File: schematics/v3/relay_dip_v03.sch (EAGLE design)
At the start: 51 parts, among them IC1 74HCT04D, P1 696-SML-0805ICTR, P2 696-SML-0805ICTR, P3 696-SML-0805ICTR, P4 696-SML-0805ICTR, U1 DS2431P+T&R

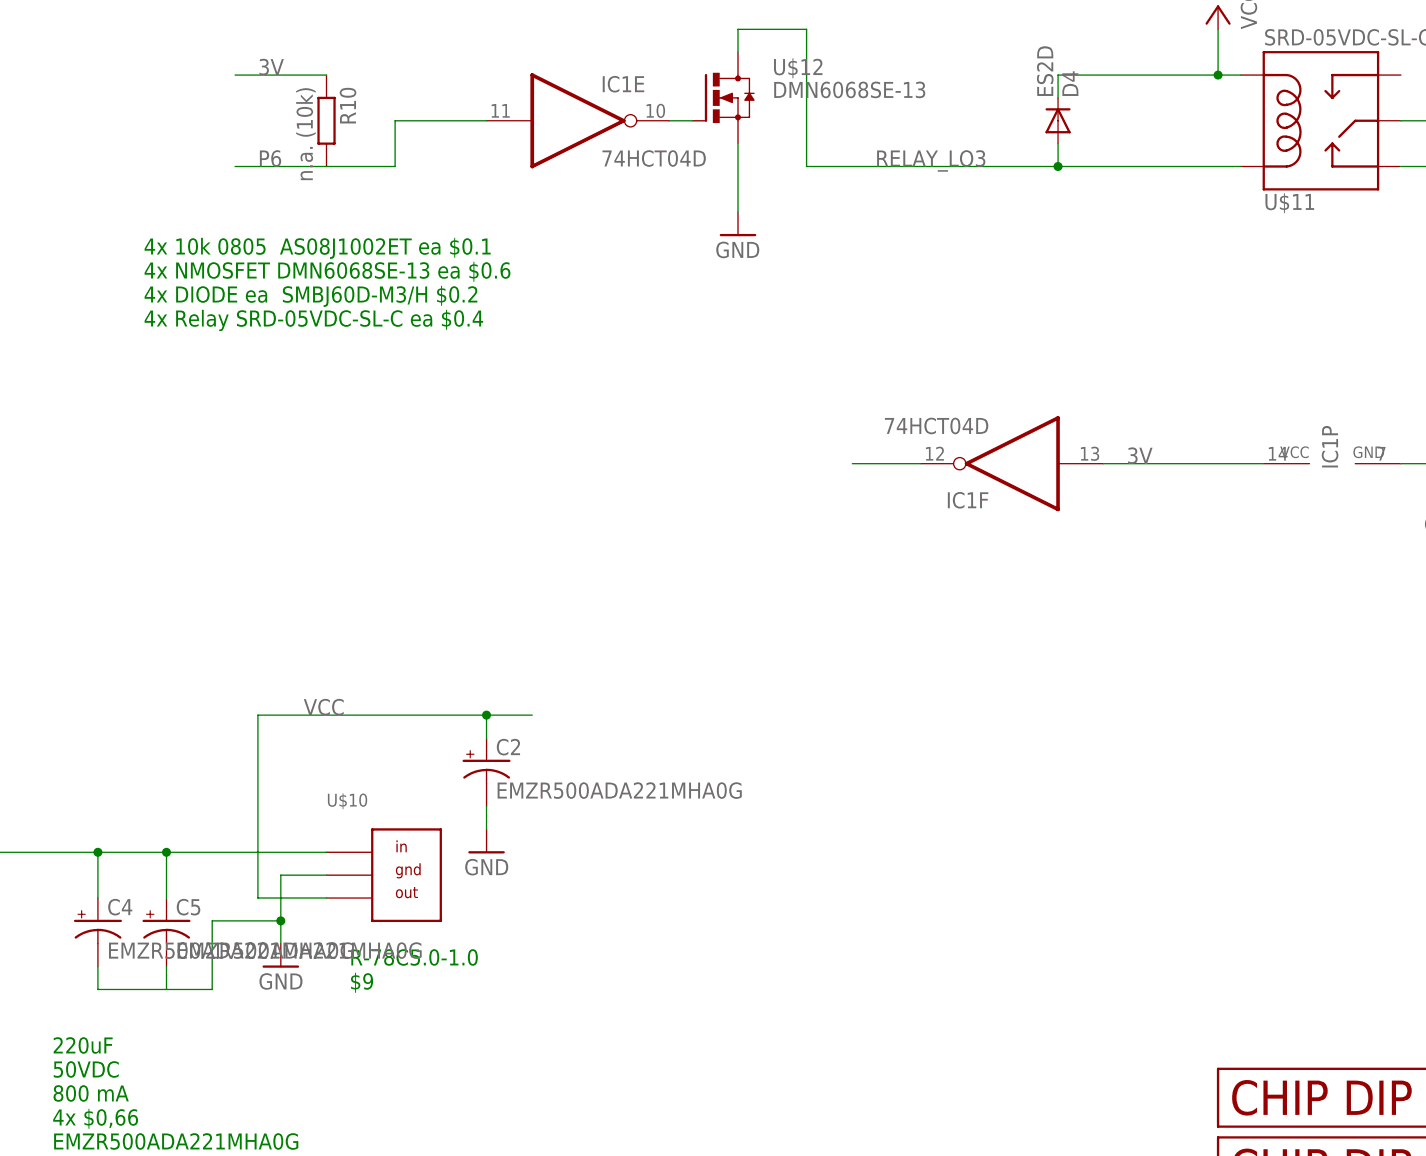
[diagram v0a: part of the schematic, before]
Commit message: added v3, fixed ds2431 footprint, added quotation
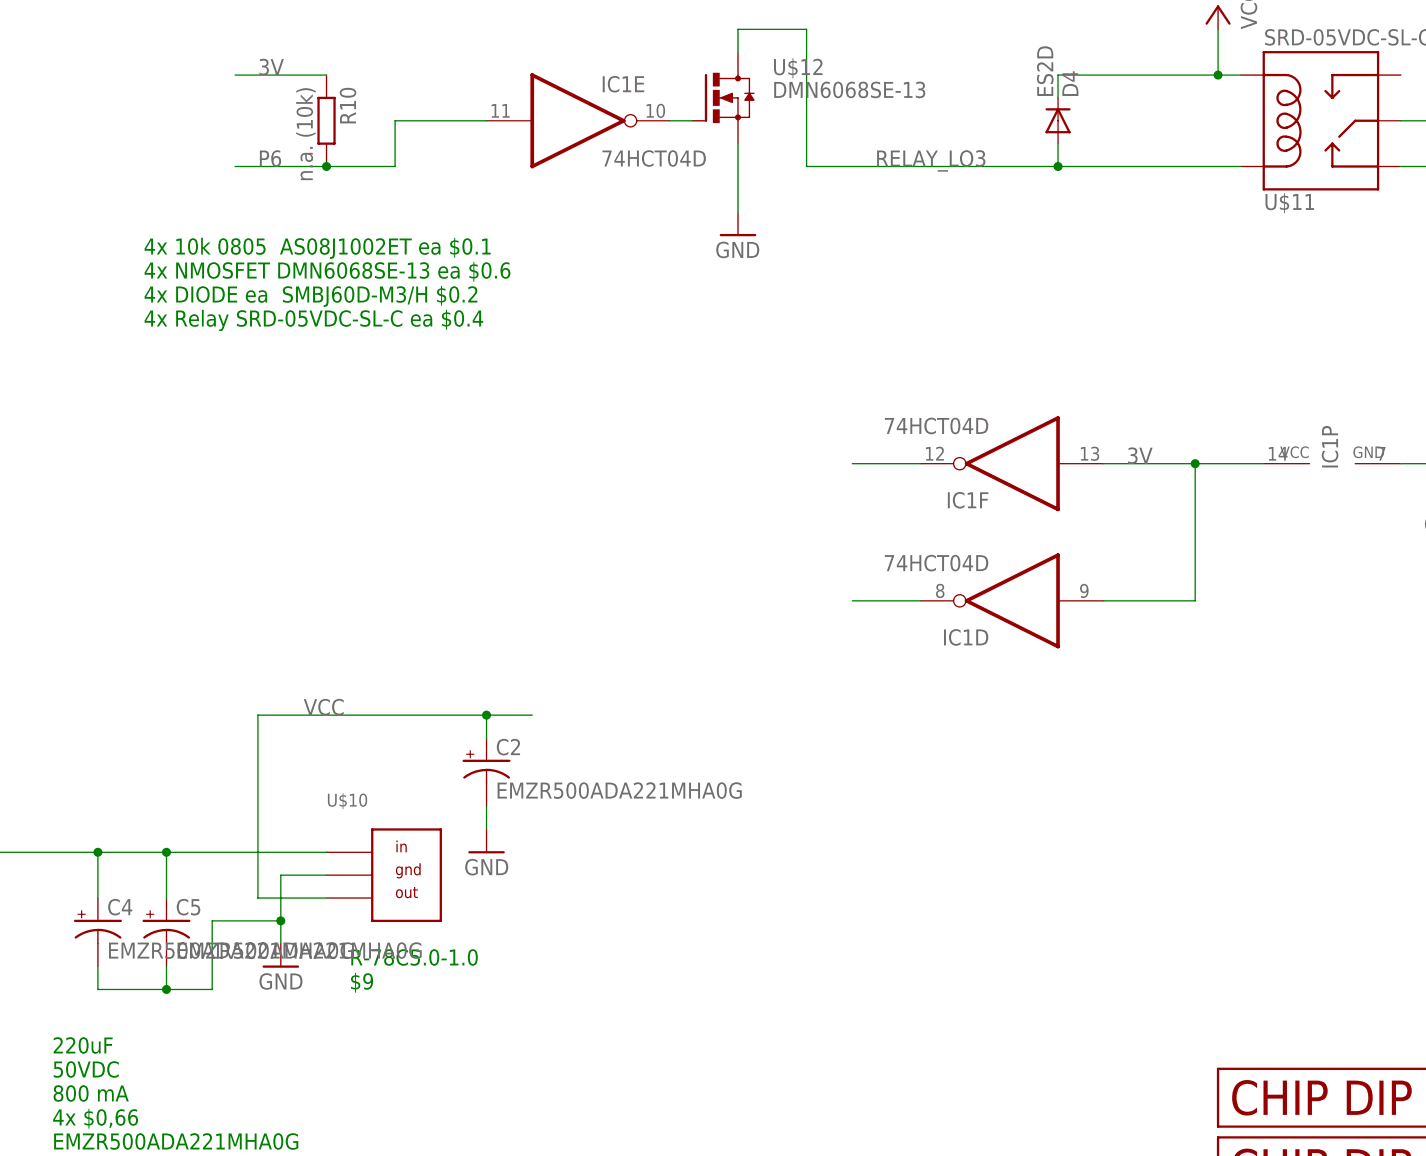
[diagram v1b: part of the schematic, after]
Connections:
- new net N$12: IC1D.O
- net 3V: now also IC1D.I
- net LD2: now also U1.IO
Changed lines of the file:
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@@
 <instance part="GND8" gate="1" x="195.58" y="414.02"/>
 <instance part="U1" gate="G$1" x="20.32" y="457.2" rot="MR0"/>
+<instance part="IC1" gate="D" x="147.32" y="403.86" rot="R180"/>
 </instances>
 <busses>
@@
 <wire x1="58.42" y1="368.3" x2="66.04" y2="368.3" width="0.1524" layer="91"/>
 <junction x="66.04" y="368.3"/>
+<junction x="53.34" y="360.68"/>
 </segment>
 <segment>
@@
 <junction x="2.54" y="459.74"/>
 <pinref part="JP1" gate="G$1" pin="2"/>
+<pinref part="U1" gate="G$1" pin="IO"/>
 </segment>
 </net>
@@
 <wire x1="71.12" y1="452.12" x2="60.96" y2="452.12" width="0.1524" layer="91"/>
 <label x="63.5" y="452.12" size="1.778" layer="95"/>
+<junction x="71.12" y="452.12"/>
 </segment>
 </net>
@@
 <segment>
 <pinref part="IC1" gate="P" pin="VCC"/>
-<wire x1="175.26" y1="419.1" x2="157.48" y2="419.1" width="0.1524" layer="91"/>
+<wire x1="175.26" y1="419.1" x2="167.64" y2="419.1" width="0.1524" layer="91"/>
 <label x="160.02" y="419.1" size="1.778" layer="95"/>
 <pinref part="IC1" gate="F" pin="I"/>
+<pinref part="IC1" gate="D" pin="I"/>
+<wire x1="167.64" y1="419.1" x2="157.48" y2="419.1" width="0.1524" layer="91"/>
+<wire x1="157.48" y1="403.86" x2="167.64" y2="403.86" width="0.1524" layer="91"/>
+<wire x1="167.64" y1="403.86" x2="167.64" y2="419.1" width="0.1524" layer="91"/>
+<junction x="167.64" y="419.1"/>
 </segment>
 </net>
@@
 </segment>
 </net>
+<net name="N$12" class="0">
+<segment>
+<pinref part="IC1" gate="D" pin="O"/>
+<wire x1="137.16" y1="403.86" x2="129.54" y2="403.86" width="0.1524" layer="91"/>
+</segment>
+</net>

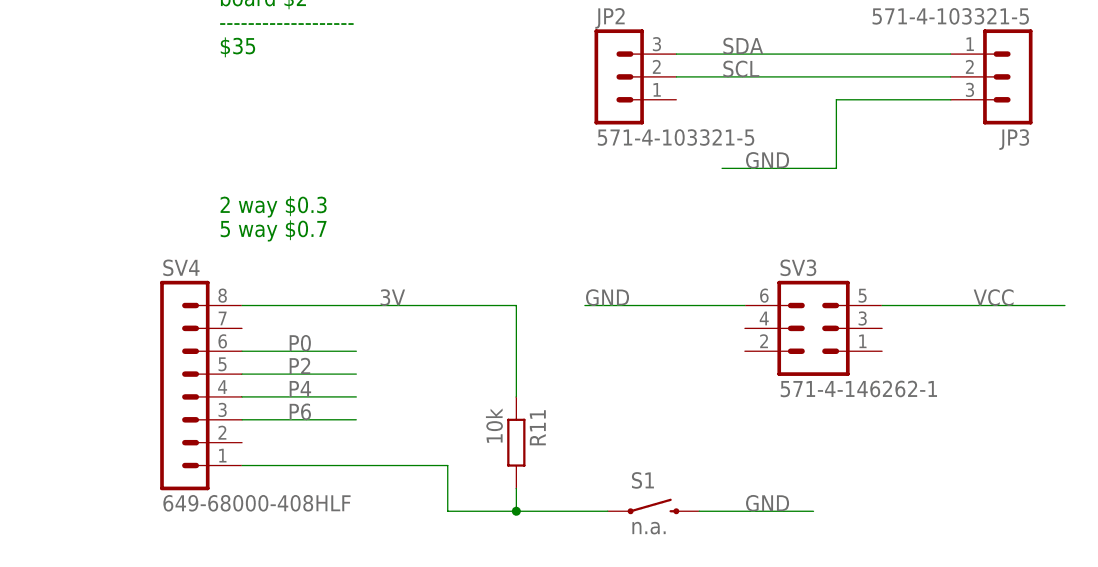
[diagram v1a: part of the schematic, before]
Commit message: flipped pin header to lower layer
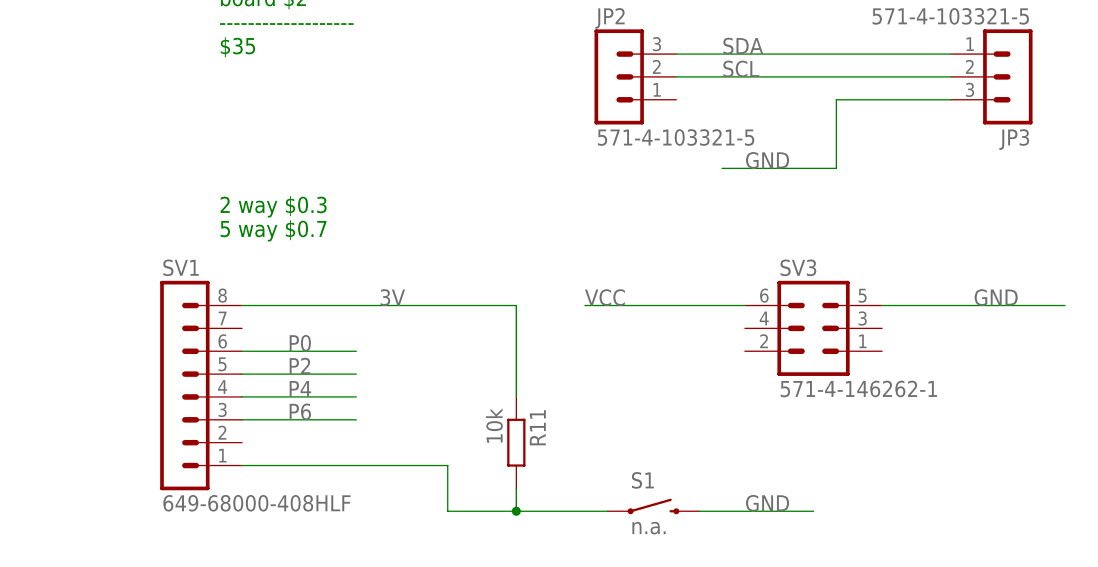
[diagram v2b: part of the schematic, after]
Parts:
- renumbered SV4 to SV1
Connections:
- net GND: now also SV3.5; no longer SV3.6
- net VCC: now also SV3.6; no longer SV3.5
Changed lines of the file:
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@@
 <part name="S1" library="SparkFun-Electromechanical" deviceset="SWITCH-MOMENTARY-2" device="SMD" value="n.a."/>
 <part name="R11" library="rcl" deviceset="R-EU_" device="R0805" value="10k"/>
-<part name="SV4" library="con-lstb" deviceset="MA08-1" device="" value="649-68000-408HLF"/>
 <part name="JP2" library="con-lstb" deviceset="MA03-1" device="" value="571-4-103321-5"/>
 <part name="JP3" library="con-lstb" deviceset="MA03-1" device="" value="571-4-103321-5"/>
@@
 <part name="GND8" library="supply1" deviceset="GND" device=""/>
 <part name="U1" library="JKW_CHIP" deviceset="DS2431" device="P" value="DS2431P+T&amp;R"/>
+<part name="SV1" library="con-lstb" deviceset="MA08-1" device="" value="649-68000-408HLF"/>
 </parts>
 <sheets>
@@
 <instance part="S1" gate="G$1" x="299.72" y="500.38"/>
 <instance part="R11" gate="G$1" x="284.48" y="508" rot="R270"/>
-<instance part="SV4" gate="1" x="246.38" y="513.08"/>
 <instance part="JP2" gate="G$1" x="294.64" y="548.64"/>
 <instance part="JP3" gate="G$1" x="340.36" y="548.64" rot="R180"/>
@@
 <instance part="U1" gate="G$1" x="20.32" y="457.2" rot="MR0"/>
 <instance part="IC1" gate="D" x="147.32" y="403.86" rot="R180"/>
+<instance part="SV1" gate="1" x="246.38" y="513.08"/>
 </instances>
 <busses>
@@
 </segment>
 <segment>
-<pinref part="SV3" gate="1" pin="6"/>
-<wire x1="309.88" y1="523.24" x2="292.1" y2="523.24" width="0.1524" layer="91"/>
-<label x="292.1" y="523.24" size="1.778" layer="95"/>
-</segment>
-<segment>
 <pinref part="GND7" gate="1" pin="GND"/>
 <pinref part="C2" gate="G$1" pin="-"/>
@@
 <wire x1="195.58" y1="419.1" x2="190.5" y2="419.1" width="0.1524" layer="91"/>
 </segment>
+<segment>
+<pinref part="SV3" gate="1" pin="5"/>
+<wire x1="325.12" y1="523.24" x2="345.44" y2="523.24" width="0.1524" layer="91"/>
+<label x="335.28" y="523.24" size="1.778" layer="95"/>
+</segment>
 </net>
 <net name="P0" class="0">
@@
 <wire x1="254" y1="518.16" x2="266.7" y2="518.16" width="0.1524" layer="91"/>
 <label x="259.08" y="518.16" size="1.778" layer="95"/>
-<pinref part="SV4" gate="1" pin="6"/>
+<pinref part="SV1" gate="1" pin="6"/>
 </segment>
 <segment>
@@
 </segment>
 <segment>
-<pinref part="SV3" gate="1" pin="5"/>
-<wire x1="325.12" y1="523.24" x2="345.44" y2="523.24" width="0.1524" layer="91"/>
-<label x="335.28" y="523.24" size="1.778" layer="95"/>
-</segment>
-<segment>
 <pinref part="U$10" gate="G$1" pin="OUT"/>
 <wire x1="71.12" y1="370.84" x2="63.5" y2="370.84" width="0.1524" layer="91"/>
@@
 <wire x1="88.9" y1="388.62" x2="88.9" y2="391.16" width="0.1524" layer="91"/>
 <junction x="88.9" y="391.16"/>
+</segment>
+<segment>
+<pinref part="SV3" gate="1" pin="6"/>
+<wire x1="309.88" y1="523.24" x2="292.1" y2="523.24" width="0.1524" layer="91"/>
+<label x="292.1" y="523.24" size="1.778" layer="95"/>
 </segment>
 </net>
@@
 <wire x1="254" y1="515.62" x2="266.7" y2="515.62" width="0.1524" layer="91"/>
 <label x="259.08" y="515.62" size="1.778" layer="95"/>
-<pinref part="SV4" gate="1" pin="5"/>
+<pinref part="SV1" gate="1" pin="5"/>
 </segment>
 <segment>
@@
 <wire x1="254" y1="513.08" x2="266.7" y2="513.08" width="0.1524" layer="91"/>
 <label x="259.08" y="513.08" size="1.778" layer="95"/>
-<pinref part="SV4" gate="1" pin="4"/>
+<pinref part="SV1" gate="1" pin="4"/>
 </segment>
 <segment>
@@
 <wire x1="254" y1="510.54" x2="266.7" y2="510.54" width="0.1524" layer="91"/>
 <label x="259.08" y="510.54" size="1.778" layer="95"/>
-<pinref part="SV4" gate="1" pin="3"/>
+<pinref part="SV1" gate="1" pin="3"/>
 </segment>
 <segment>
@@
 <wire x1="284.48" y1="502.92" x2="284.48" y2="500.38" width="0.1524" layer="91"/>
 <junction x="284.48" y="500.38"/>
-<pinref part="SV4" gate="1" pin="1"/>
 <wire x1="254" y1="505.46" x2="276.86" y2="505.46" width="0.1524" layer="91"/>
 <wire x1="276.86" y1="505.46" x2="276.86" y2="500.38" width="0.1524" layer="91"/>
+<pinref part="SV1" gate="1" pin="1"/>
 </segment>
 </net>
@@
 <pinref part="R11" gate="G$1" pin="1"/>
 <wire x1="284.48" y1="523.24" x2="284.48" y2="513.08" width="0.1524" layer="91"/>
-<pinref part="SV4" gate="1" pin="8"/>
 <label x="269.24" y="523.24" size="1.778" layer="95"/>
-</segment>
-<segment>
+<pinref part="SV1" gate="1" pin="8"/>
+</segment>
+<segment>

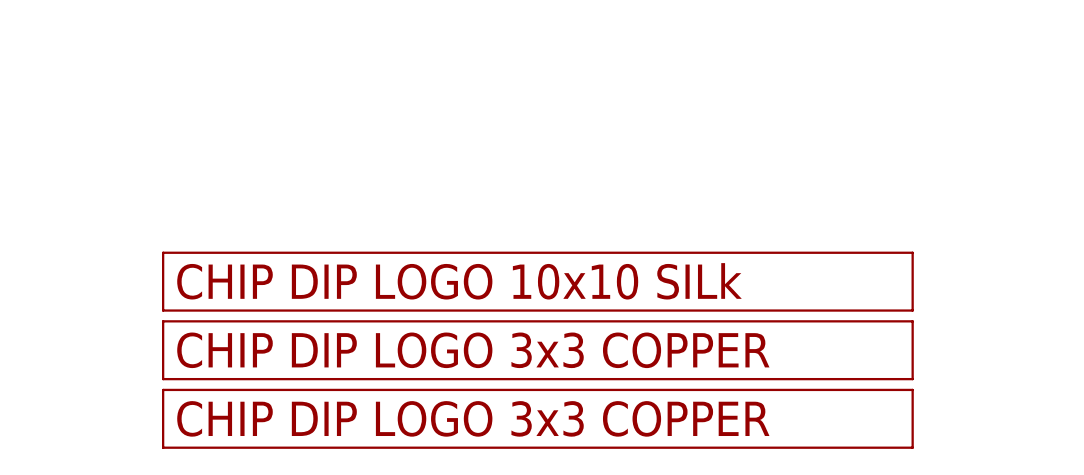
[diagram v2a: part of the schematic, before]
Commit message: added designators
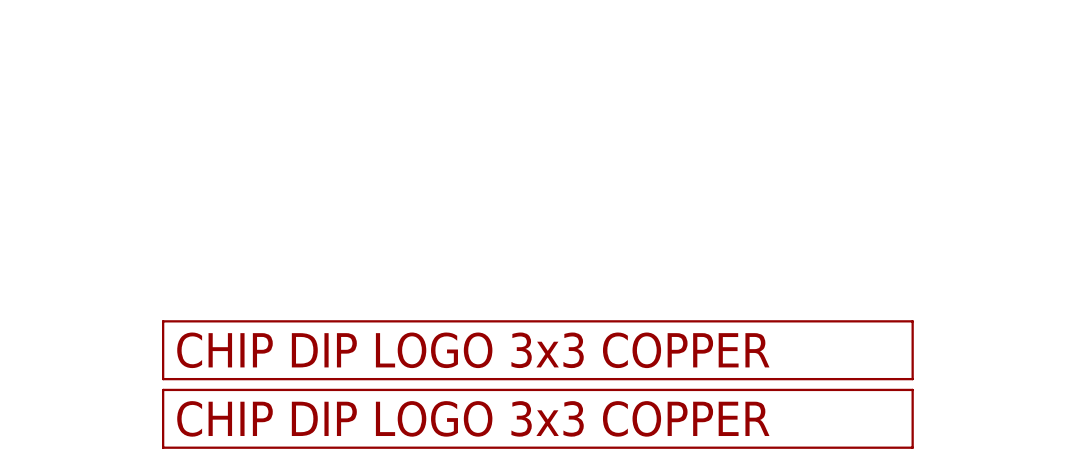
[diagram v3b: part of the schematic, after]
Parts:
- removed U$5: LOGO_10X10_SILK, logo:LOGO_10X10_SILK
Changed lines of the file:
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@@
 <?xml version="1.0" encoding="utf-8"?>
 <!DOCTYPE eagle SYSTEM "eagle.dtd">
-<eagle version="7.6.0">
+<eagle version="7.7.0">
 <drawing>
 <settings>
@@
 <part name="P1" library="led" deviceset="LED" device="CHIP-LED0805" value="696-SML-0805ICTR"/>
 <part name="R3" library="rcl" deviceset="R-EU_" device="R0805" value="200R"/>
-<part name="U$5" library="logo" deviceset="LOGO_10X10_SILK" device=""/>
 <part name="FRAME1" library="frames" deviceset="DINA3_L" device=""/>
 <part name="R8" library="rcl" deviceset="R-EU_" device="R0805" value="n.a. (10k)"/>
@@
 <instance part="P1" gate="G$1" x="309.88" y="467.36"/>
 <instance part="R3" gate="G$1" x="309.88" y="449.58" rot="R270"/>
-<instance part="U$5" gate="G$1" x="170.18" y="345.44"/>
 <instance part="FRAME1" gate="G$1" x="-30.48" y="327.66"/>
 <instance part="FRAME1" gate="G$2" x="256.54" y="327.66"/>
